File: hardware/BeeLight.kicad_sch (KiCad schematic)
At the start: 23 parts, among them IC102 APDS-9306-065, IC103 BME688, M101 BL54L15, Q101 BSS84, SW101 JOIN, X102 DEBUG

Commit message: Hardware rev 1 seems to be working
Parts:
- X102: now not fitted; now left out of the parts list
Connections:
- net SDA: now also M101.31 (P0.04); no longer M101.38 (P2.06)
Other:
- moved on the sheet: R104, R105

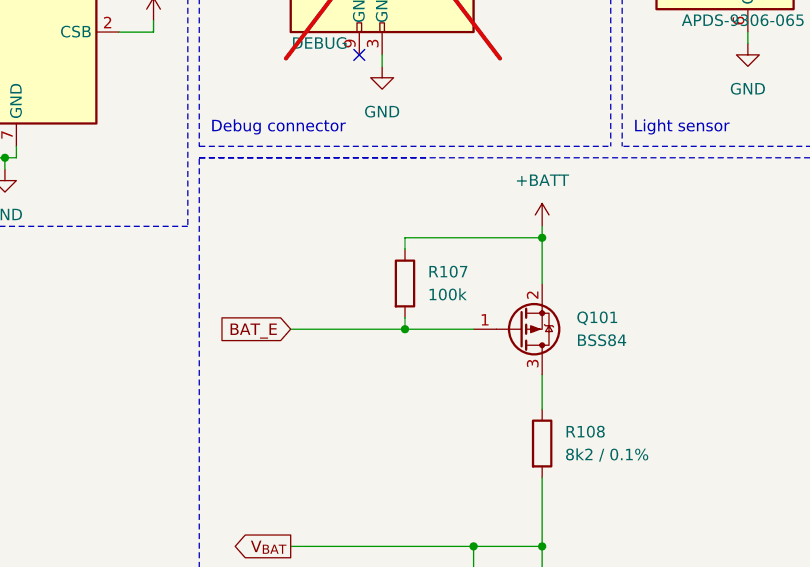
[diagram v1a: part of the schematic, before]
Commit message: Bring up hardware and firmware
- Remove old files

- Update README.md
- Update converter for z2m

- Fix typos in DTS includes
- Fix wrong patch command

- Add dimension to PCB specification Kibot output
- Add blocklist to west.yml
- Add missing mounting holes
- Add custom cluster for VOC, IAQ and CO2 for Zigbee2Mqtt
- Add patches for custom cluster for ncs-zigbee
- Add west command to build and flash the device configuration
- Add 3D files for the housing
- Add 3D printer project for the housing
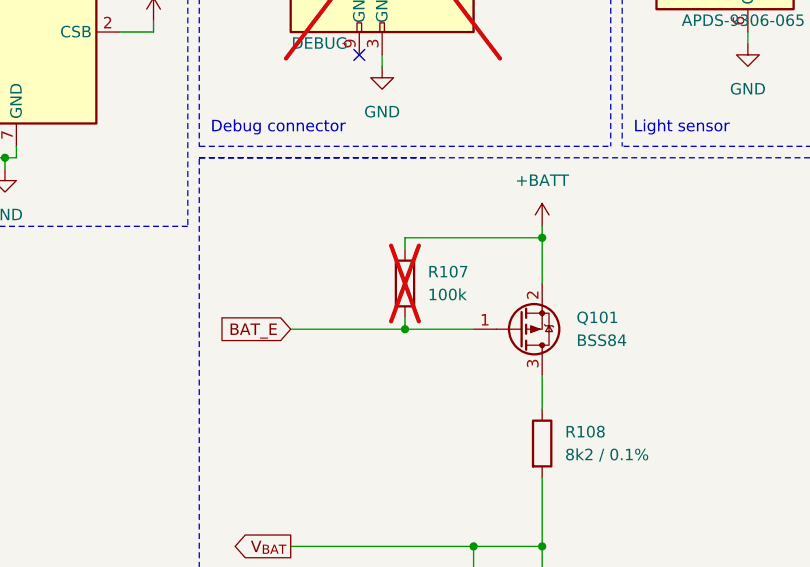
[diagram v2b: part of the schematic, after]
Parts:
- R107: now not fitted; now left out of the parts list
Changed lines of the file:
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@@
 		(unit 1)
 		(exclude_from_sim no)
-		(in_bom yes)
+		(in_bom no)
 		(on_board yes)
-		(dnp no)
+		(dnp yes)
 		(fields_autoplaced yes)
 		(property "Reference" "R107"
@@
 			(at 228.6 77.47 0)
 			(effects
+				(font
+					(size 1.27 1.27)
+				)
+				(hide yes)
+			)
+		)
+		(property "CONFIG" ""
+			(at 228.6 77.47 0)
+			(effects

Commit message: - Remove old files
- Replace nRF54 module

- Update README.md
- Update converter for z2m

- Fix typos in DTS includes
- Fix wrong patch command

- Add BME688
- Add dimension to PCB specification Kibot output
- Add blocklist to west.yml
- Add missing mounting holes
- Add custom cluster for VOC, IAQ and CO2 for Zigbee2Mqtt
- Add patches for custom cluster for ncs-zigbee
- Add west command to build and flash the device configuration
- Add 3D files for the housing
- Add 3D printer project for the housing
- Add template from Vincent
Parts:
- removed BT101: Battery_Cell, Keystone:3002, symbol Device:Battery_Cell
- removed C101, C102, C104, C105, C106: 100n, Capacitor_SMD:C_0402_1005Metric_Pad0.74x0.62mm_HandSolder, symbol Device:C_Small
- removed C103: 100n, Capacitor_SMD:C_0402_1005Metric_Pad0.74x0.62mm_HandSolder, symbol Device:C
- removed D101: IDENTIFY, LED_SMD:LED_0805_2012Metric_Pad1.15x1.40mm_HandSolder, symbol Device:LED
- removed IC102: APDS-9306-065, Broadcom:Broadcom_DFN-6_2x2mm_P0.65mm, symbol Sensor_Optical:APDS-9306-065
- removed IC103: BME688, Package_LGA_Kampi:Bosch_LGA-8_3x3mm_P0.8mm_ClockwisePinNumbering, symbol Bosch:BME688
- removed M101: BL54L15, Ezurio:BL54L15, symbol Ezurio:BL54L15
- removed Q101: BSS84, Package_TO_SOT_SMD:SOT-23-3, symbol Transistor_FET:BSS84
- removed R101, R107: 100k, Resistor_SMD:R_0402_1005Metric_Pad0.72x0.64mm_HandSolder, symbol Device:R
- removed R102: 0R, Resistor_SMD:R_0805_2012Metric_Pad1.20x1.40mm_HandSolder, symbol Device:R
- removed R103: 220R, Resistor_SMD:R_0402_1005Metric_Pad0.72x0.64mm_HandSolder, symbol Device:R
- removed R104, R105, R106: 1k8, Resistor_SMD:R_0402_1005Metric_Pad0.72x0.64mm_HandSolder, symbol Device:R
- removed R108: 8k2 / 0.1%, Resistor_SMD:R_0402_1005Metric_Pad0.72x0.64mm_HandSolder, symbol Device:R
- removed R109: 2k2 / 0.1%, Resistor_SMD:R_0402_1005Metric_Pad0.72x0.64mm_HandSolder, symbol Device:R
- removed SW101: JOIN, Wuerth:WS-TASV-6x6, symbol Switch:SW_Push
- removed X102: DEBUG, Connector_PinHeader_1.27mm:PinHeader_2x05_P1.27mm_Vertical, symbol Connector:Conn_ARM_JTAG_SWD_10
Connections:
- no-connect marks 27 -> 0
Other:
- added sheet Block Diagram (Block Diagram.kicad_sch)
- added sheet Project Architecture (Project Architecture.kicad_sch)
- added sheet Revision History (Revision History.kicad_sch)
- note added: "${BOARD_NAME}"
- note added: "${RELEASE_DATE_NUM}"
- note added: "${SHEET_NAME_10}"
- note added: "${SHEET_NAME_11}"
- note added: "${SHEET_NAME_12}"
- note added: "${SHEET_NAME_13}"
- note added: "${SHEET_NAME_14}"
- note added: "${SHEET_NAME_15}"
- note added: "${SHEET_NAME_16}"
- note added: "${SHEET_NAME_17}"
- note added: "${SHEET_NAME_18}"
- note added: "${SHEET_NAME_19}"
- note added: "${SHEET_NAME_1}"
- note added: "${SHEET_NAME_20}"
- note added: "${SHEET_NAME_21}"
- note added: "${SHEET_NAME_22}"
- note added: "${SHEET_NAME_23}"
- note added: "${SHEET_NAME_24}"
- note added: "${SHEET_NAME_25}"
- note added: "${SHEET_NAME_26}"
- note added: "${SHEET_NAME_27}"
- note added: "${SHEET_NAME_28}"
- note added: "${SHEET_NAME_29}"
- note added: "${SHEET_NAME_2}"
- note added: "${SHEET_NAME_30}"
- note added: "${SHEET_NAME_31}"
- note added: "${SHEET_NAME_32}"
- note added: "${SHEET_NAME_33}"
- note added: "${SHEET_NAME_34}"
- note added: "${SHEET_NAME_35}"
- note added: "${SHEET_NAME_36}"
- note added: "${SHEET_NAME_37}"
- note added: "${SHEET_NAME_38}"
- note added: "${SHEET_NAME_39}"
- note added: "${SHEET_NAME_3}"
- note added: "${SHEET_NAME_40}"
- note added: "${SHEET_NAME_4}"
- note added: "${SHEET_NAME_5}"
- note added: "${SHEET_NAME_6}"
- note added: "${SHEET_NAME_7}"
- note added: "${SHEET_NAME_8}"
- note added: "${SHEET_NAME_9}"
- note added: "1"
- note added: "10"
- note added: "11"
- note added: "12"
- note added: "13"
- note added: "14"
- note added: "15"
- note added: "16"
- note added: "17"
- note added: "18"
- note added: "19"
- note added: "2"
- note added: "20"
- note added: "21"
- note added: "22"
- note added: "23"
- note added: "24"
- note added: "25"
- note added: "26"
- note added: "27"
- note added: "28"
- note added: "29"
- note added: "3"
- note added: "30"
- note added: "31"
- note added: "32"
- note added: "33"
- note added: "34"
- note added: "35"
- note added: "36"
- note added: "37"
- note added: "38"
- note added: "39"
- note added: "4"
- note added: "40"
- note added: "5"
- note added: "6"
- note added: "7"
- note added: "8"
- note added: "9"
- note added: "BOTTOM VIEW"
- note added: "CHECKED - There shouldn't be any mistakes. Contact the engineer if you find any."
- note added: "Comment"
- note added: "DESIGN CONSIDERATIONS"
- note added: "DRAFT - Very early stage of schematic, ignore details."
- note added: "Date: ${RELEASE_DATE}"
- note added: "Index"
- note added: "NOTES"
- note added: "Not fitted components are marked as"
- note added: "PRELIMINARY - Close to final schematic."
- note added: "Page"
- note added: "RELEASED - A board with this schematic has been sent to production."
- note added: "Rev ${REVISION}"
- note added: "TOP VIEW"
- note added: "Variant: ${VARIANT}"
- note removed: "Battery measurement"
- note removed: "Debug connector"
- note removed: "Gas, Pressure, Temperature & Humidity"
- note removed: "Light sensor"
- note removed: "NOTE: The nRF54 has an internal reference of ±0.6 V."
- note removed: "Power supply"
- company: (none) -> ${COMPANY}

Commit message: Implement new CI/CD workflow
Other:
- title: BeeLight v2 -> (none)
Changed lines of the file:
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@@
 	(paper "A3")
 	(title_block
-		(title "BeeLight v2")
 		(date "2025-06-05")
 		(rev "${REVISION}")

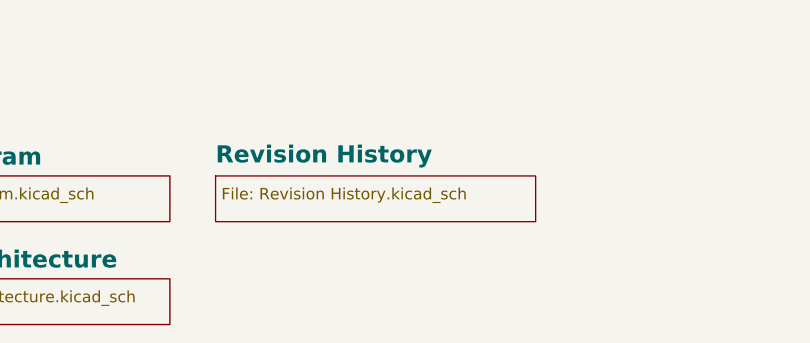
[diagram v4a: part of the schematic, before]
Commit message: - Change ADC filter capacitor to 1 nF - Update documentation with current consumption - Update CI/CD pipeline
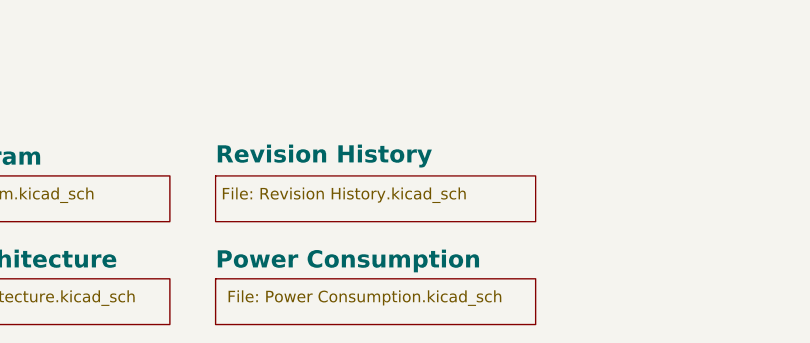
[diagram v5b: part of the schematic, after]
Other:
- added sheet Power Consumption (Power Consumption.kicad_sch)
- title: (none) -> Cover Page
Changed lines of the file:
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@@
 	(paper "A3")
 	(title_block
+		(title "Cover Page")
 		(date "2025-06-05")
 		(rev "${REVISION}")
@@
 				)
 			)
+		)
+	)
+	(sheet
+		(at 346.71 314.96)
+		(size 35.56 5.08)
+		(exclude_from_sim no)
+		(in_bom yes)
+		(on_board yes)
+		(dnp no)
+		(stroke
+			(width 0.1524)
+			(type solid)
+		)
+		(fill
+			(color 0 0 0 0.0000)
+		)
+		(property "Sheetname" "Power Consumption"
+			(at 346.71 313.9309 0)
+			(effects
+				(font
+					(face "Times New Roman")
+					(size 1.905 1.905)
+					(bold yes)
+					(color 0 0 0 1)
+				)
+				(justify left bottom)
+			)
+		)
+		(property "Sheetfile" "Power Consumption.kicad_sch"
+			(at 347.98 316.23 0)
+			(effects
+				(font
+					(face "Arial")
+					(size 1.27 1.27)
+				)
+				(justify left top)
+			)
+		)
+		(instances
+			(project "BeeLight"
+				(path "/d5742f03-3b1a-42e5-a384-018bd4b919aa"
+					(page "6")
+				)
+			)
